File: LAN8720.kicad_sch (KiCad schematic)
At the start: 1 part, among them U2 LAN8720A

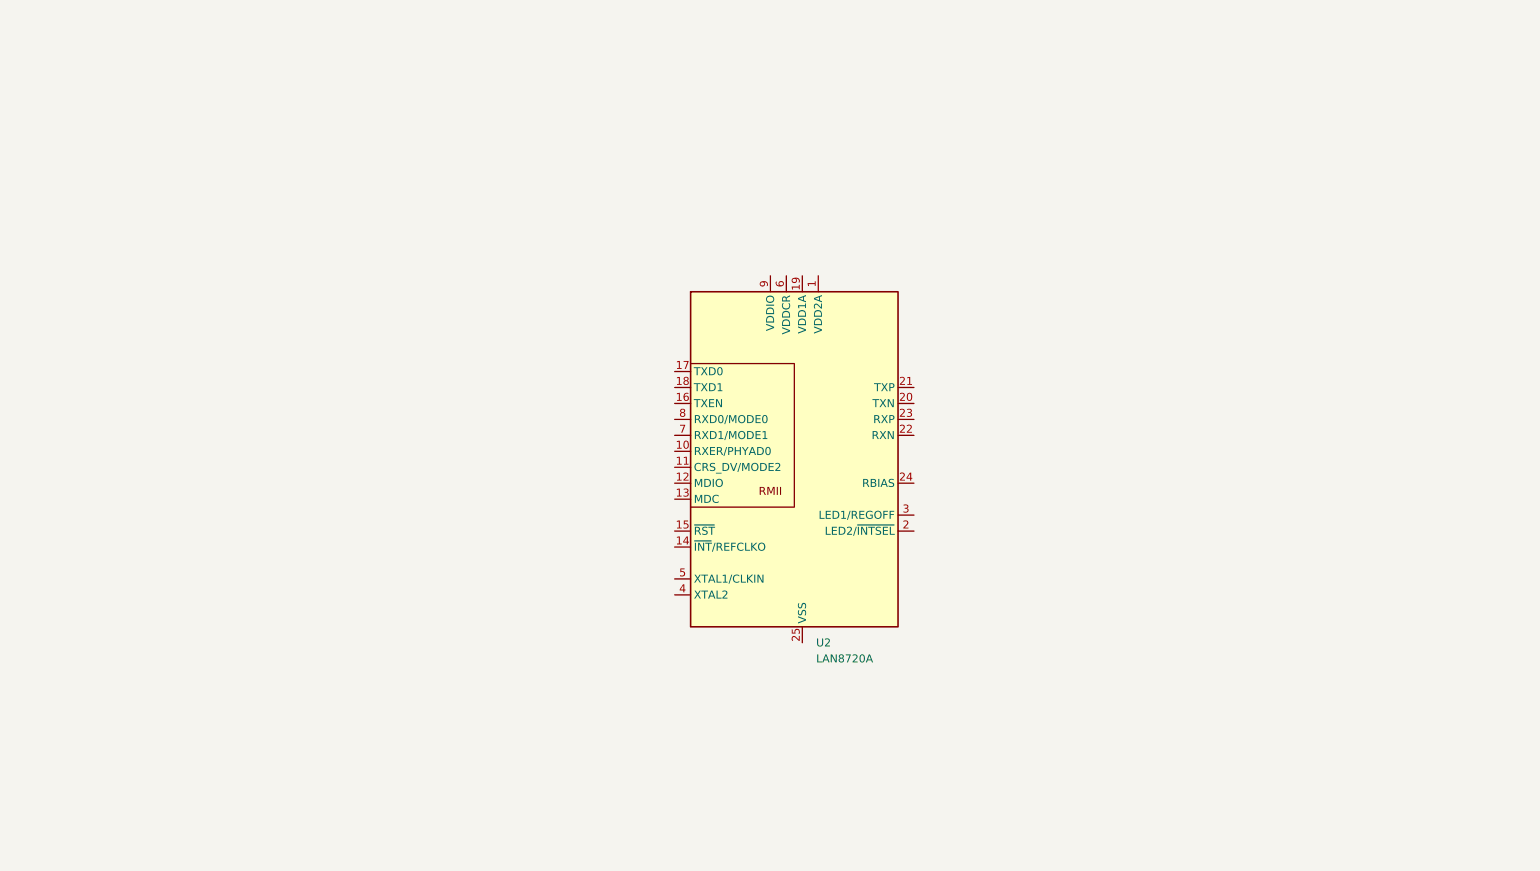
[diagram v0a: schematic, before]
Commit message: Correct pins in schematics and add LAN8270
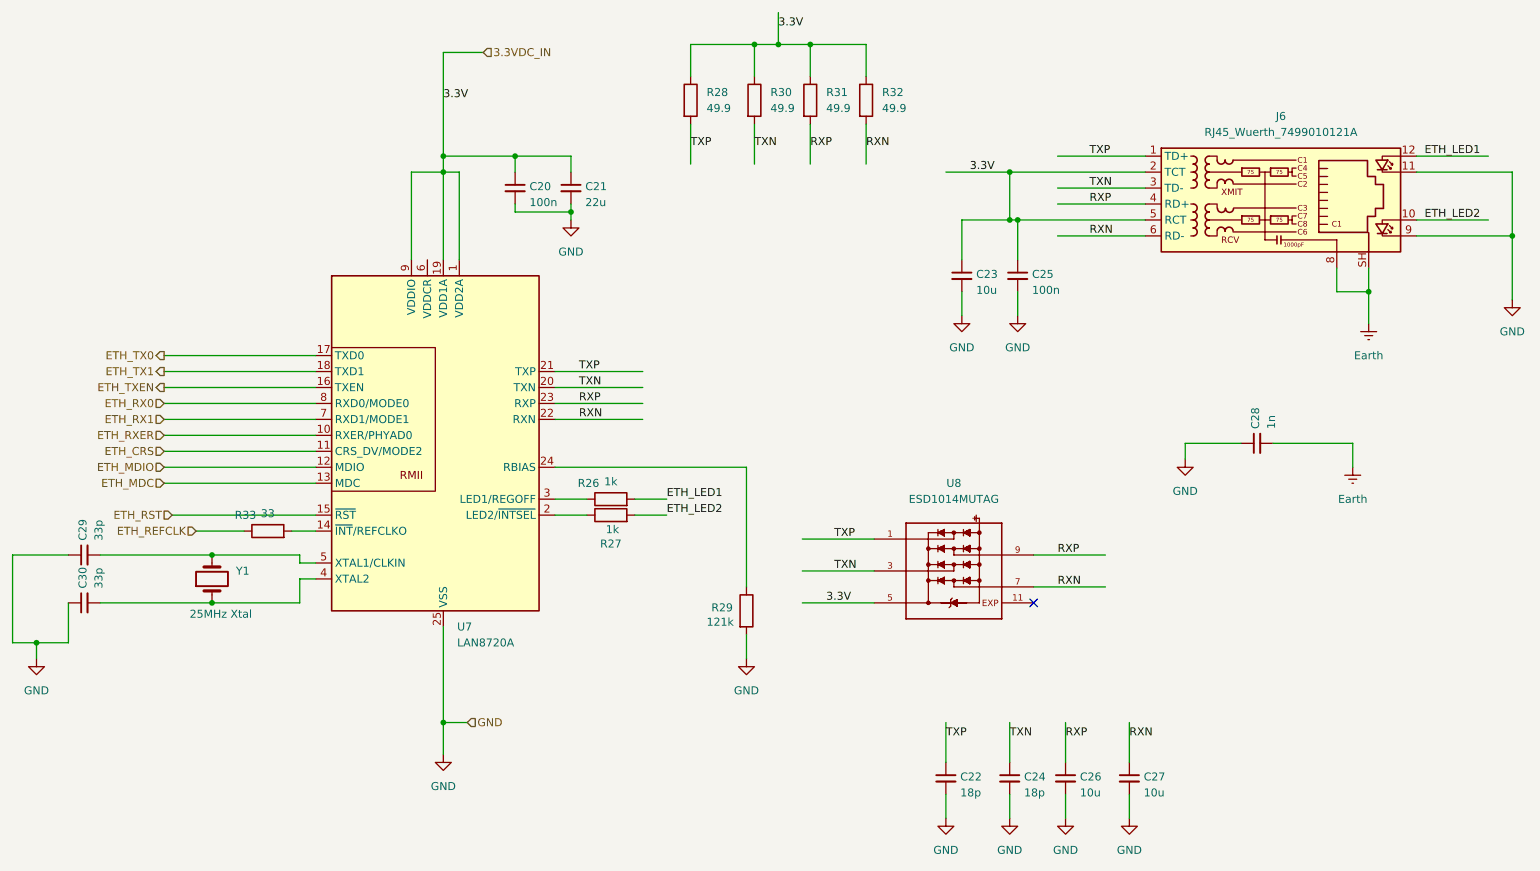
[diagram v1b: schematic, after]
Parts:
- removed U2: LAN8720A, Package_DFN_QFN:VQFN-24-1EP_4x4mm_P0.5mm_EP2.5x2.5mm_ThermalVias, symbol Interface_Ethernet:LAN8720A
- added C20, C25: 100n, Capacitor_SMD:C_0402_1005Metric_Pad0.74x0.62mm_HandSolder, symbol Device:C_Small
- added C21: 22u, Capacitor_SMD:C_0402_1005Metric_Pad0.74x0.62mm_HandSolder, symbol Device:C_Small
- added C22, C24: 18p, Capacitor_SMD:C_0402_1005Metric_Pad0.74x0.62mm_HandSolder, symbol Device:C_Small
- added C23, C26, C27: 10u, Capacitor_SMD:C_0402_1005Metric_Pad0.74x0.62mm_HandSolder, symbol Device:C_Small
- added C28: 1n, Capacitor_SMD:C_0402_1005Metric_Pad0.74x0.62mm_HandSolder, symbol Device:C_Small
- added C29, C30: 33p, Capacitor_SMD:C_0402_1005Metric_Pad0.74x0.62mm_HandSolder, symbol Device:C_Small
- added J6: RJ45_Wuerth_7499010121A, Connector_RJ:RJ45_Wuerth_7499010121A_Horizontal, symbol Connector:RJ45_Wuerth_7499010121A
- added R26, R27: 1k, symbol Device:R
- added R28, R30, R31, R32: 49.9, symbol Device:R
- added R29: 121k, symbol Device:R
- added R33: 33, symbol Device:R
- added U7: LAN8720A, Package_DFN_QFN:VQFN-24-1EP_4x4mm_P0.5mm_EP2.5x2.5mm_ThermalVias, symbol Interface_Ethernet:LAN8720A
- added U8: ESD1014MUTAG, ESD1014MUTAG:SON50P260X260X55-11N, symbol ESD1014MUTAG:ESD1014MUTAG
- added Y1: 25MHz Xtal, symbol Device:Crystal
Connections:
- new net: C30.2, U7.4 (XTAL2), Y1.1
- new net: C29.2, U7.5 (XTAL1/CLKIN), Y1.2
- new net: R27.1, U7.2 (LED2/~{INTSEL})
- new net: R29.1, U7.24 (RBIAS)
- new net: R26.1, U7.3 (LED1/REGOFF)
- new net: R33.2, U7.14 (~{INT}/REFCLKO)
- new net 3.3VDC_IN: C20.1, C21.1, C23.1, C25.1, J6.2 (TCT), J6.5 (RCT), R28.1, R30.1, R31.1, R32.1, U7.1 (VDD2A), U7.19 (VDD1A), U7.9 (VDDIO), U8.5
- new net ETH_CRS: U7.11 (CRS_DV/MODE2)
- new net ETH_LED1: J6.12, R26.2
- new net ETH_LED2: J6.10, R27.2
- new net ETH_MDC: U7.13 (MDC)
- new net ETH_MDIO: U7.12 (MDIO)
- new net ETH_REFCLK: R33.1
- new net ETH_RST: U7.15 (~{RST})
- new net ETH_RX0: U7.8 (RXD0/MODE0)
- new net ETH_RX1: U7.7 (RXD1/MODE1)
- new net ETH_RXER: U7.10 (RXER/PHYAD0)
- new net ETH_TX0: U7.17 (TXD0)
- new net ETH_TX1: U7.18 (TXD1)
- new net ETH_TXEN: U7.16 (TXEN)
- new net Earth: C28.2, J6.8, J6.SH
- new net GND: C20.2, C21.2, C22.2, C23.2, C24.2, C25.2, C26.2, C27.2, C28.1, C29.1, C30.1, J6.11, J6.9, R29.2, U7.25 (VSS)
- new net RXN: C27.1, J6.6 (RD-), R32.2, U7.22 (RXN), U8.7
- new net RXP: C26.1, J6.4 (RD+), R31.2, U7.23 (RXP), U8.9
- new net TXN: C24.1, J6.3 (TD-), R30.2, U7.20 (TXN), U8.3
- new net TXP: C22.1, J6.1 (TD+), R28.2, U7.21 (TXP), U8.1
- no-connect marks 0 -> 1
